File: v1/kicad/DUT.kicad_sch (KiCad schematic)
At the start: 6 parts, among them J12 228-1290-00-0602J, J13 Heavy-duty, J14 Banana Jack, J15 Banana Jack, J16 Banana Jack, J17 Conn_01x03_Socket

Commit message: Added power connector
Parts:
- removed J17: Conn_01x03_Socket, symbol Connector:Conn_01x03_Socket
- added J10: 1718757, symbol Connector:Screw_Terminal_01x03
- added J7: 39-01-2040, symbol Connector:Conn_01x04_Socket
- J12: value 228-1290-00-0602J -> 228-1277-00-0602J; footprint 28655410 -> (none)
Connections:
- net B: now also J10.1 (Pin_1), J7.2 (Pin_2)
- net C: now also J10.3 (Pin_3), J7.4 (Pin_4)
- net E: now also J10.2 (Pin_2), J7.3 (Pin_3)
- new net GUARD: J7.1 (Pin_1)

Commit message: Adding KiKit multiboarding
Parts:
- removed J10: 1718757, symbol Connector:Screw_Terminal_01x03
- removed J7: 39-01-2040, symbol Connector:Conn_01x04_Socket
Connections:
- net B: now also J13.2 (L2); no longer J13.3 (L3)
- net C: now also J13.3 (L3); no longer J13.2 (L2)

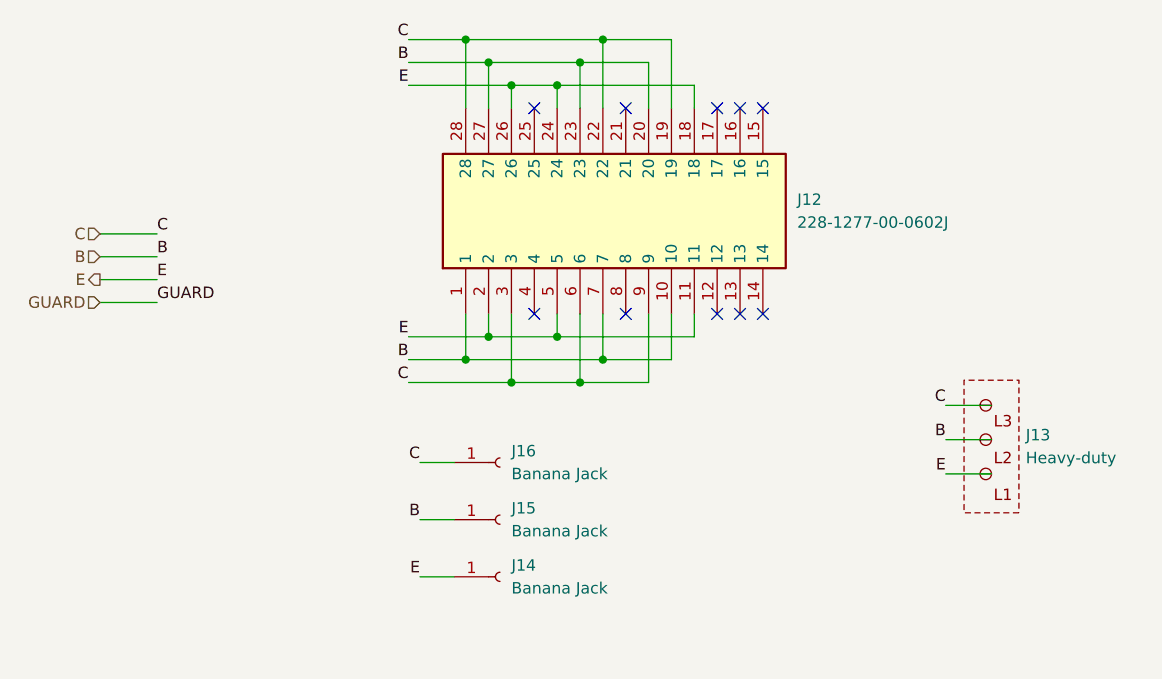
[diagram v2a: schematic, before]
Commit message: Fixed mistakes with the polarity of some caps
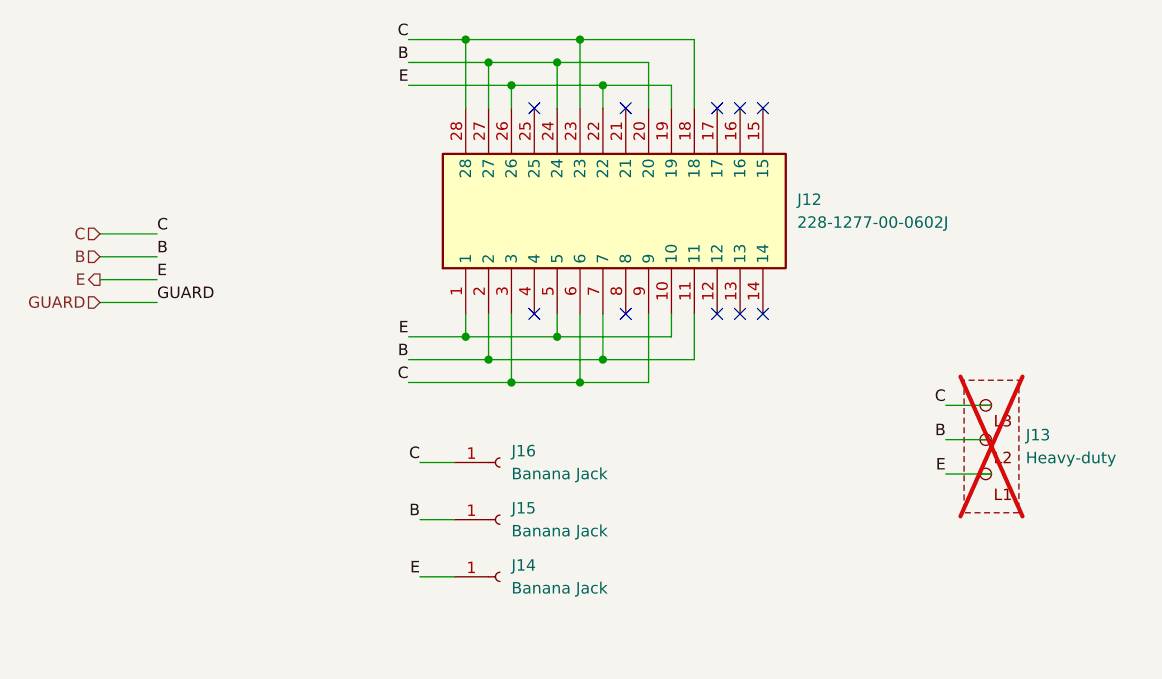
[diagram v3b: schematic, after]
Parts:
- J13: now not fitted
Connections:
- net B: now also J12.11, J12.2, J12.24; no longer J12.1, J12.10, J12.23
- net C: now also J12.18, J12.23; no longer J12.19, J12.22
- net E: now also J12.1, J12.10, J12.19, J12.22; no longer J12.11, J12.18, J12.2, J12.24

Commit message: Fixed mistakes and made making a BOM easier
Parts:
- added J20: Heavy-duty, symbol custom:3-Pin-Socket_Basic
- J12: Height 12.07 -> (none); Manufacturer_Name ARIES -> (none); Manufacturer_Part_Number 28-6554-10 -> (none); Mouser Part Number 535-28-6554-10 -> (none); Mouser Price/Stock https://www.mouser.co.uk/ProductDetail/Aries-Electronics/28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 -> (none); Spend (none) -> $$$
- J13: Spend (none) -> $$$; now fitted
- J14, J15, J16: Spend (none) -> $$$
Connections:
- net B: now also J20.3 (L3)
- net C: now also J20.2 (L2)
- net E: now also J20.1 (L1)
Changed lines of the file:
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@@
+	(wire
+		(pts
+			(xy 139.7 86.36) (xy 144.78 86.36)
+		)
+		(stroke
+			(width 0)
+			(type default)
+		)
+	)
 	(wire
 		(pts
@@
 	(wire
 		(pts
+			(xy 139.7 90.17) (xy 144.78 90.17)
+		)
+		(stroke
+			(width 0)
+			(type default)
+		)
+	)
+	(wire
+		(pts
 			(xy 81.28 88.9) (xy 85.09 88.9)
 		)
@@
 		(pts
 			(xy 81.28 82.55) (xy 85.09 82.55)
+		)
+		(stroke
+			(width 0)
+			(type default)
+		)
+	)
+	(wire
+		(pts
+			(xy 139.7 93.98) (xy 144.78 93.98)
 		)
 		(stroke
@@
 	)
 	(label "C"
+		(at 139.7 90.17 180)
+		(effects
+			(font
+				(size 1.27 1.27)
+			)
+			(justify right bottom)
+		)
+	)
+	(label "C"
 		(at 80.01 29.21 180)
 		(effects
@@
 		)
 	)
+	(label "B"
+		(at 139.7 86.36 180)
+		(effects
+			(font
+				(size 1.27 1.27)
+			)
+			(justify right bottom)
+		)
+	)
 	(label "E"
 		(at 81.28 88.9 180)
@@
 	(label "C"
 		(at 80.01 67.31 180)
+		(effects
+			(font
+				(size 1.27 1.27)
+			)
+			(justify right bottom)
+		)
+	)
+	(label "E"
+		(at 139.7 93.98 180)
 		(effects
 			(font
@@
 		(on_board yes)
 		(in_pos_files yes)
-		(dnp yes)
+		(dnp no)
 		(fields_autoplaced yes)
 		(property "Reference" "J13"
@@
 		)
 		(property "Description" ""
+			(at 144.78 73.66 0)
+			(hide yes)
+			(show_name no)
+			(do_not_autoplace no)
+			(effects
+				(font
+					(size 1.27 1.27)
+				)
+			)
+		)
+		(property "Spend" "$$$"
 			(at 144.78 73.66 0)
 			(hide yes)
@@
 			)
 		)
-		(property "Datasheet" "https://www.arieselec.com/wp-content/uploads/2020/02/10001-universal-dip-zif-test-socket.pdf"
+		(property "Datasheet" ""
 			(at 281.28 40.64 0)
 			(hide yes)
@@
 			)
 		)
-		(property "Description" "Aries Electronics 2.54mm Pitch 28 Way Through Hole Universal ZIF Test Socket"
+		(property "Description" ""
 			(at 86.36 59.69 0)
 			(hide yes)
@@
 			)
 		)
-		(property "Height" "12.07"
+		(property "Height" ""
 			(at 481.28 40.64 0)
 			(hide yes)
@@
 			)
 		)
-		(property "Manufacturer_Name" "ARIES"
+		(property "Manufacturer_Name" ""
 			(at 581.28 40.64 0)
 			(hide yes)
@@
 			)
 		)
-		(property "Manufacturer_Part_Number" "28-6554-10"
+		(property "Manufacturer_Part_Number" ""
 			(at 681.28 40.64 0)
 			(hide yes)
@@
 			)
 		)
-		(property "Mouser Part Number" "535-28-6554-10"
+		(property "Mouser Part Number" ""
 			(at 781.28 40.64 0)
 			(hide yes)
@@
 			)
 		)
-		(property "Mouser Price/Stock" "https://www.mouser.co.uk/ProductDetail/Aries-Electronics/28-6554-10?qs=WZRMhwwaLl%2FXVzQUw3ZSkA%3D%3D"
+		(property "Mouser Price/Stock" ""
 			(at 881.28 40.64 0)
 			(hide yes)
@@
 				)
 				(justify left top)
+			)
+		)
+		(property "Spend" "$$$"
+			(at 86.36 59.69 90)
+			(hide yes)
+			(show_name no)
+			(do_not_autoplace no)
+			(effects
+				(font
+					(size 1.27 1.27)
+				)
 			)
 		)
@@
 			)
 		)
-		(property "Description" "Generic connector, single row, 01x01, script generated"
+		(property "Description" ""
+			(at 90.17 76.2 0)
+			(hide yes)
+			(show_name no)
+			(do_not_autoplace no)
+			(effects
+				(font
+					(size 1.27 1.27)
+				)
+			)
+		)
+		(property "Spend" "$$$"
 			(at 90.17 76.2 0)
 			(hide yes)
@@
 			)
 		)
-		(property "Description" "Generic connector, single row, 01x01, script generated"
+		(property "Description" ""
+			(at 90.17 82.55 0)
+			(hide yes)
+			(show_name no)
+			(do_not_autoplace no)
+			(effects
+				(font
+					(size 1.27 1.27)
+				)
+			)
+		)
+		(property "Spend" "$$$"
 			(at 90.17 82.55 0)
 			(hide yes)
@@
 				(path "/d7a5a570-e509-45ae-a7d3-ba88e6083368/cd41930f-a470-4d4a-ba14-5ff26eaaa2fd"
 					(reference "J15")
+					(unit 1)
+				)
+			)
+		)
+	)
+	(symbol
+		(lib_id "custom:3-Pin-Socket_Basic")
+		(at 144.78 90.17 180)
+		(unit 1)
+		(body_style 1)
+		(exclude_from_sim no)
+		(in_bom yes)
+		(on_board yes)
+		(in_pos_files yes)
+		(dnp no)
+		(fields_autoplaced yes)
+		(property "Reference" "J20"
+			(at 148.59 89.6619 0)
+			(show_name no)
+			(do_not_autoplace no)
+			(effects
+				(font
+					(size 1.27 1.27)
+				)
+				(justify right)
+			)
+		)
+		(property "Value" "Heavy-duty"
+			(at 148.59 92.2019 0)
+			(show_name no)
+			(do_not_autoplace no)
+			(effects
+				(font
+					(size 1.27 1.27)
+				)
+				(justify right)
+			)
+		)
+		(property "Footprint" ""
+			(at 144.78 90.17 0)
+			(hide yes)
+			(show_name no)
+			(do_not_autoplace no)
+			(effects
+				(font
+					(size 1.27 1.27)
+				)
+			)
+		)
+		(property "Datasheet" ""
+			(at 144.78 90.17 0)
+			(hide yes)
+			(show_name no)
+			(do_not_autoplace no)
+			(effects
+				(font
+					(size 1.27 1.27)
+				)
+			)
+		)
+		(property "Description" ""
+			(at 144.78 90.17 0)
+			(hide yes)
+			(show_name no)
+			(do_not_autoplace no)
+			(effects
+				(font
+					(size 1.27 1.27)
+				)
+			)
+		)
+		(property "Spend" "$$$"
+			(at 144.78 90.17 0)
+			(hide yes)
+			(show_name no)
+			(do_not_autoplace no)
+			(effects
+				(font
+					(size 1.27 1.27)
+				)
+			)
+		)
+		(pin "3"
+		)
+		(pin "1"
+		)
+		(pin "2"
+		)
+		(instances
+			(project "Charakterograf"
+				(path "/d7a5a570-e509-45ae-a7d3-ba88e6083368/cd41930f-a470-4d4a-ba14-5ff26eaaa2fd"
+					(reference "J20")
 					(unit 1)
 				)
@@
 			)
 		)
-		(property "Description" "Generic connector, single row, 01x01, script generated"
+		(property "Description" ""
 			(at 90.17 88.9 0)
 			(hide yes)
+			(show_name no)
+			(do_not_autoplace no)
+			(effects
+				(font
+					(size 1.27 1.27)
+				)
+			)
+		)
+		(property "Spend" "$$$"
+			(at 90.17 88.9 0)
+			(hide yes)
